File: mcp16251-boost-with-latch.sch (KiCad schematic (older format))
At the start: 26 parts

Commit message: Battery input SPDT switch
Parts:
- added SW?: SW_SPDT, symbol Switch:SW_SPDT
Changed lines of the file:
@@
 	1    0    0    1
 $EndComp
-Text GLabel 1500 1900 0    50   Input ~ 0
+Text GLabel 1100 2000 0    50   Input ~ 0
 VBAT_RAW
 Text GLabel 1900 4300 2    50   Input ~ 0
@@
 	1800 5600 1600 5600
 Connection ~ 1800 4900
+$Comp
+L Switch:SW_SPDT SW?
+U 1 1 5C07AA94
+P 1300 2000
+F 0 "SW?" H 1300 2290 50  0000 C CNN
+F 1 "SW_SPDT" H 1300 2197 50  0000 C CNN
+F 2 "" H 1300 2000 50  0001 C CNN
+F 3 "" H 1300 2000 50  0001 C CNN
+	1    1300 2000
+	1    0    0    -1
+$EndComp
 $EndSCHEMATC

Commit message: Create and assign footprints.
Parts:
- added JP1: Jumper, MCP16251_module:R_0805_HS, symbol Jumper:SolderJumper_2_Open
- C1, C2, C3, C4: renamed from C?; footprint (none) -> MCP16251_module:R_1206_HS
- C5: renamed from C?; footprint (none) -> MCP16251_module:R_0805_HS
- J1: renamed from J?; footprint (none) -> MCP16251_module:Conn_01x02_cast
- J2, J3: renamed from J?; footprint (none) -> MCP16251_module:Conn_01x02_cast_mirrored
- J4, J5, J6, J7, J8: renamed from J?; footprint (none) -> MCP16251_module:SMD-Pad_01x01
- J9: renamed from J?; footprint (none) -> Connectors_JST:JST_PH_S2B-PH-K_02x2.00mm_Angled
- L1: renamed from L?; footprint (none) -> MCP16251_module:L_Taiyo-Yuden_NR-S-40xx_HS
- Q1: renamed from Q?; footprint (none) -> MCP16251_module:SOT-23_HS
- Q2: renamed from Q?; value 2N3904 -> NPN_3904; footprint (none) -> MCP16251_module:SOT-23_HS
- R1, R2, R3, R4, R5, R6: renamed from R?; footprint (none) -> MCP16251_module:R_0805_HS
- RV1: renamed from RV?; footprint (none) -> MCP16251_module:Conn_01x03_small
- SW1: renamed from SW?; footprint (none) -> MCP16251_module:Conn_01x03_small
- SW2: renamed from SW?; footprint (none) -> Buttons_Switches_SMD:SW_SPST_TL3342
- U1: renamed from U?; footprint (none) -> MCP16251_module:SOT-23-6_HS
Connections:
- wire segments 64 -> 71
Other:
- moved on the sheet: SW1

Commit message: Bugfixes
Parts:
- J3: footprint MCP16251_module:Conn_01x02_cast_mirrored -> MCP16251_module:Conn_01x01_cast
- Q2: symbol Device:Q_NPN_EBC -> Device:Q_NPN_BEC
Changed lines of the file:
@@
 $EndComp
 $Comp
-L Device:Q_NPN_EBC Q2
+L Device:Q_NPN_BEC Q2
 U 1 1 5C03897A
 P 3300 2700
@@
 F 0 "J3" H 6379 4342 50  0000 L CNN
 F 1 "THT_Castellated" H 6379 4249 50  0000 L CNN
-F 2 "MCP16251_module:Conn_01x02_cast_mirrored" H 6300 4300 50  0001 C CNN
+F 2 "MCP16251_module:Conn_01x01_cast" H 6300 4300 50  0001 C CNN
 F 3 "~" H 6300 4300 50  0001 C CNN
 	1    6300 4300

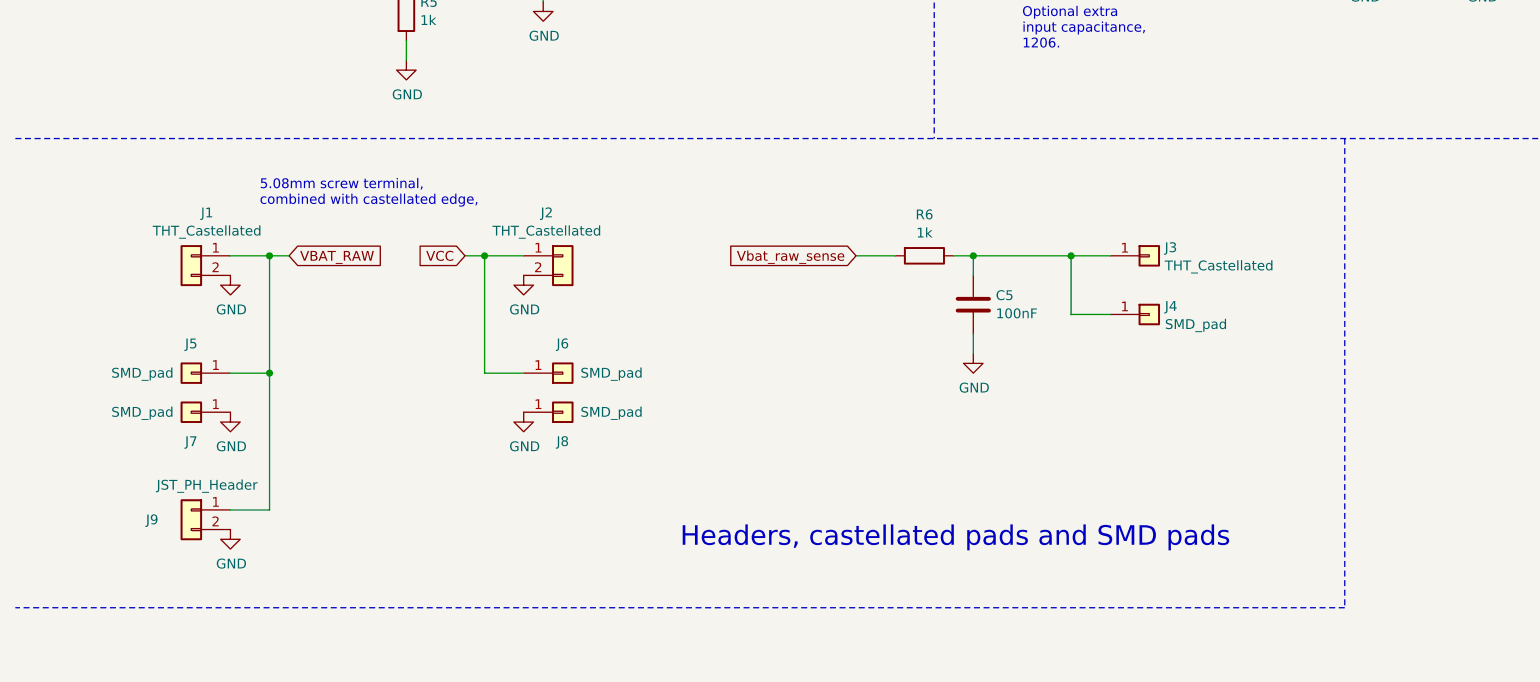
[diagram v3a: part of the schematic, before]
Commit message: Try alternative (more square-ish) layout
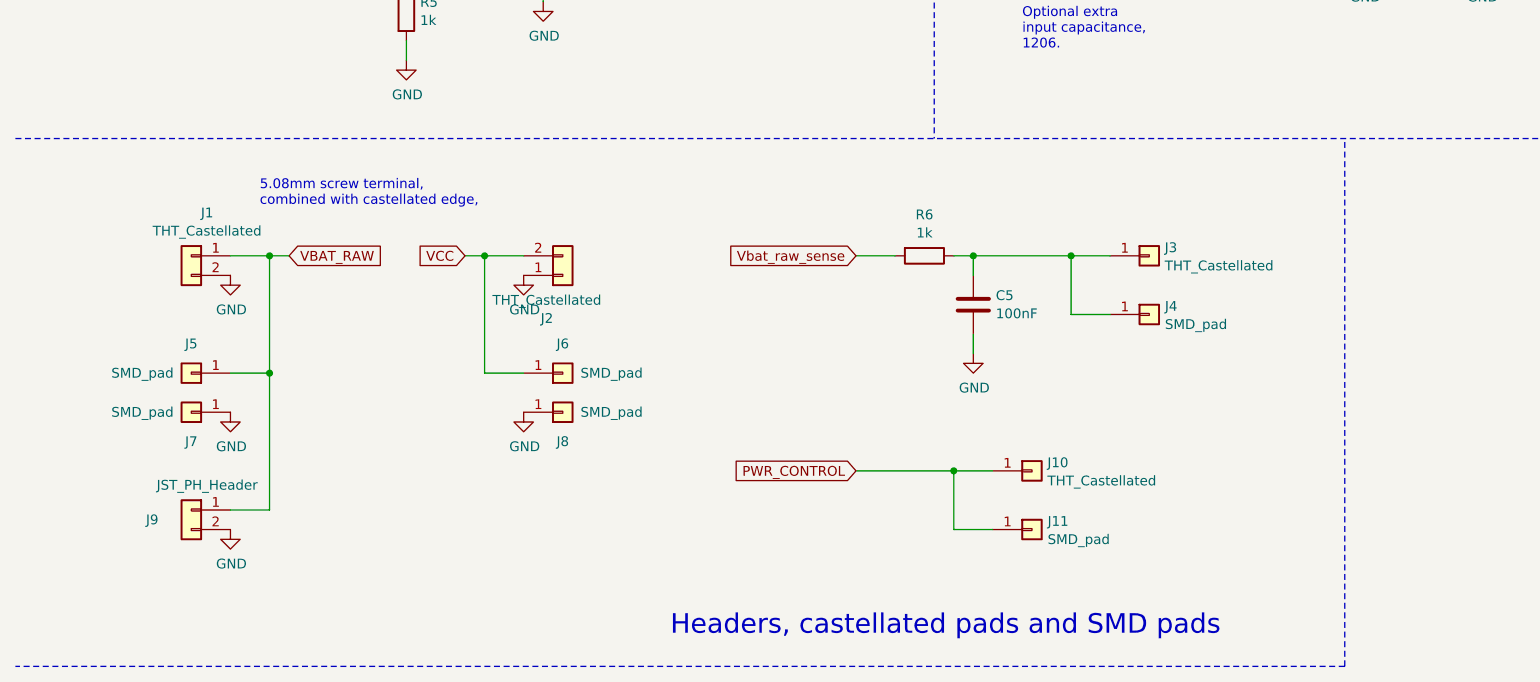
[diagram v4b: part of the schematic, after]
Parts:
- added J10: THT_Castellated, MCP16251_module:Conn_01x01_cast, symbol Connector_Generic:Conn_01x01
- added J11: SMD_pad, MCP16251_module:SMD-Pad_01x01, symbol Connector_Generic:Conn_01x01
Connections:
- net GND: now also J2.1 (Pin_1); no longer J2.2 (Pin_2)
- net PWR_CONTROL: now also J10.1 (Pin_1), J11.1 (Pin_1)
- net VCC: now also J2.2 (Pin_2); no longer J2.1 (Pin_1)
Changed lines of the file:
@@
 L Connector_Generic:Conn_01x02 J2
 U 1 1 5C0585BB
-P 3300 4300
-F 0 "J2" H 3219 4520 50  0000 C CNN
-F 1 "THT_Castellated" H 3219 4427 50  0000 C CNN
-F 2 "MCP16251_module:Conn_01x02_cast_mirrored" H 3300 4300 50  0001 C CNN
-F 3 "~" H 3300 4300 50  0001 C CNN
-	1    3300 4300
-	1    0    0    -1
+P 3300 4400
+F 0 "J2" H 3219 4620 50  0000 C CNN
+F 1 "THT_Castellated" H 3219 4527 50  0000 C CNN
+F 2 "MCP16251_module:Conn_01x02_cast_mirrored" H 3300 4400 50  0001 C CNN
+F 3 "~" H 3300 4400 50  0001 C CNN
+	1    3300 4400
+	1    0    0    1
 $EndComp
 $Comp
@@
 Wire Wire Line
 	2900 4300 3100 4300
-Text Notes 3900 5800 0    100  ~ 0
+Text Notes 3850 6250 0    100  ~ 0
 Headers, castellated pads and SMD pads
 Wire Notes Line
-	7300 3700 7300 6100
-Wire Notes Line
-	7300 6100 500  6100
+	7300 6400 500  6400
 $Comp
 L Connector_Generic:Conn_01x02 J9
@@
 Wire Wire Line
 	1600 1700 1800 1700
+Text GLabel 4800 5400 0    50   Input ~ 0
+PWR_CONTROL
+$Comp
+L Connector_Generic:Conn_01x01 J10
+U 1 1 5C08B0BD
+P 5700 5400
+F 0 "J10" H 5779 5442 50  0000 L CNN
+F 1 "THT_Castellated" H 5779 5349 50  0000 L CNN
+F 2 "MCP16251_module:Conn_01x01_cast" H 5700 5400 50  0001 C CNN
+F 3 "~" H 5700 5400 50  0001 C CNN
+	1    5700 5400
+	1    0    0    -1
+$EndComp
+$Comp
+L Connector_Generic:Conn_01x01 J11
+U 1 1 5C08B0C3
+P 5700 5700
+F 0 "J11" H 5780 5742 50  0000 L CNN
+F 1 "SMD_pad" H 5780 5649 50  0000 L CNN
+F 2 "MCP16251_module:SMD-Pad_01x01" H 5700 5700 50  0001 C CNN
+F 3 "~" H 5700 5700 50  0001 C CNN
+	1    5700 5700
+	1    0    0    -1
+$EndComp
+Wire Wire Line
+	4800 5400 5300 5400
+Wire Wire Line
+	5300 5400 5300 5700
+Wire Wire Line
+	5300 5700 5500 5700
+Connection ~ 5300 5400
+Wire Wire Line
+	5300 5400 5500 5400
+Wire Notes Line
+	7300 6400 7300 3700
 $EndSCHEMATC

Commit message: Include voltage supervisors for reliable start and battery protection
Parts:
- removed C3: CP1, MCP16251_module:R_1206_HS, symbol Device:CP1
- added F?: Polyfuse, symbol Device:Polyfuse
- added J?: THT_Castellated, MCP16251_module:Conn_01x01_cast, symbol Connector_Generic:Conn_01x01
- added J?: SMD_pad, MCP16251_module:SMD-Pad_01x01, symbol Connector_Generic:Conn_01x01
- added Q? (x4): Q_PMOS_GSD, symbol Device:Q_PMOS_GSD
- added Q?: Q_NPN_BEC, symbol Device:Q_NPN_BEC
- added R? (x5): 100k, MCP16251_module:R_0805_HS, symbol Device:R_Small
- added U?: MIC809, symbol _Project_Local:MIC809
- added U?: MIC803, symbol _Project_Local:MIC803
- added U? (x2): Opamp_Dual_Generic, symbol Device:Opamp_Dual_Generic
- R4: symbol Device:R -> Device:R_Small
- R5: value 1k -> 100k; symbol Device:R -> Device:R_Small
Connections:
- net GND: now also SW2.1, Q?.2 (E), R?.2, U?.1 (GND), U?.1 (GND), U?.4 (V-)
- net PWR_CONTROL: now also R5.1
- net VBAT: now also U?.3 (VCC); no longer U1.3 (EN)
- net VBAT_RAW: now also F?.2; no longer JP1.1 (A), SW1.2 (B)
- net VCC renamed 5V
- net 5V: now also R?.1, U?.2 (-), U?.3 (VCC)
- new net: F?.1, JP1.1 (A), SW1.2 (B)
- new net: Q?.1 (G), Q?.1 (G), R?.1, U?.1
- new net: Q?.1 (G), Q?.1 (G), Q?.3 (C), R?.1
- new net: Q?.2 (S), Q?.2 (S), R?.2 (x2)
- new net: Q?.1 (B), R?.1
- new net: R?.2, R?.2
- new net 3-4.2V: Q?.3 (D), Q?.3 (D), U?.3 (+), U?.8 (V+)
- new net STAGE1: R?.1, U1.3 (EN), U?.2 (~RST)
- new net STAGE2: J?.1 (Pin_1), J?.1 (Pin_1), U?.2 (~RST)
- new net uC_ADC: Q?.3 (D), Q?.3 (D)
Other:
- note added: "750mA\n1206"
- note added: "Power supply headers,\ncastellated and SMD pads"
- note added: "Power-on/off\ncontrol header"
- note added: "Raw VBAT input, power-off circuit,\nvoltage supervisor for boost converter"
- note added: "THT_Castellated = 5.08mm screw terminal,\ncombined with castellated edge"
- note added: "TODO: needs fixing!"
- note added: "To RESET pin on microcontroller"
- note added: "Voltage supervisor for microcontroller"
- note added: "Vth = 2.93V"
- note added: "open-drain"
- note added: "or 10uF"
- note removed: "5.08mm screw terminal,\ncombined with castellated edge,"
- note removed: "Headers, castellated pads and SMD pads"
- note removed: "Optional extra\ninput capacitance,\n1206."
- note removed: "Raw VBAT input, voltage sense\nand auto power-off"
- moved on the sheet: C1, C2, C4, C5, J1, J10, J11, J2, J3, J4, J5, J6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

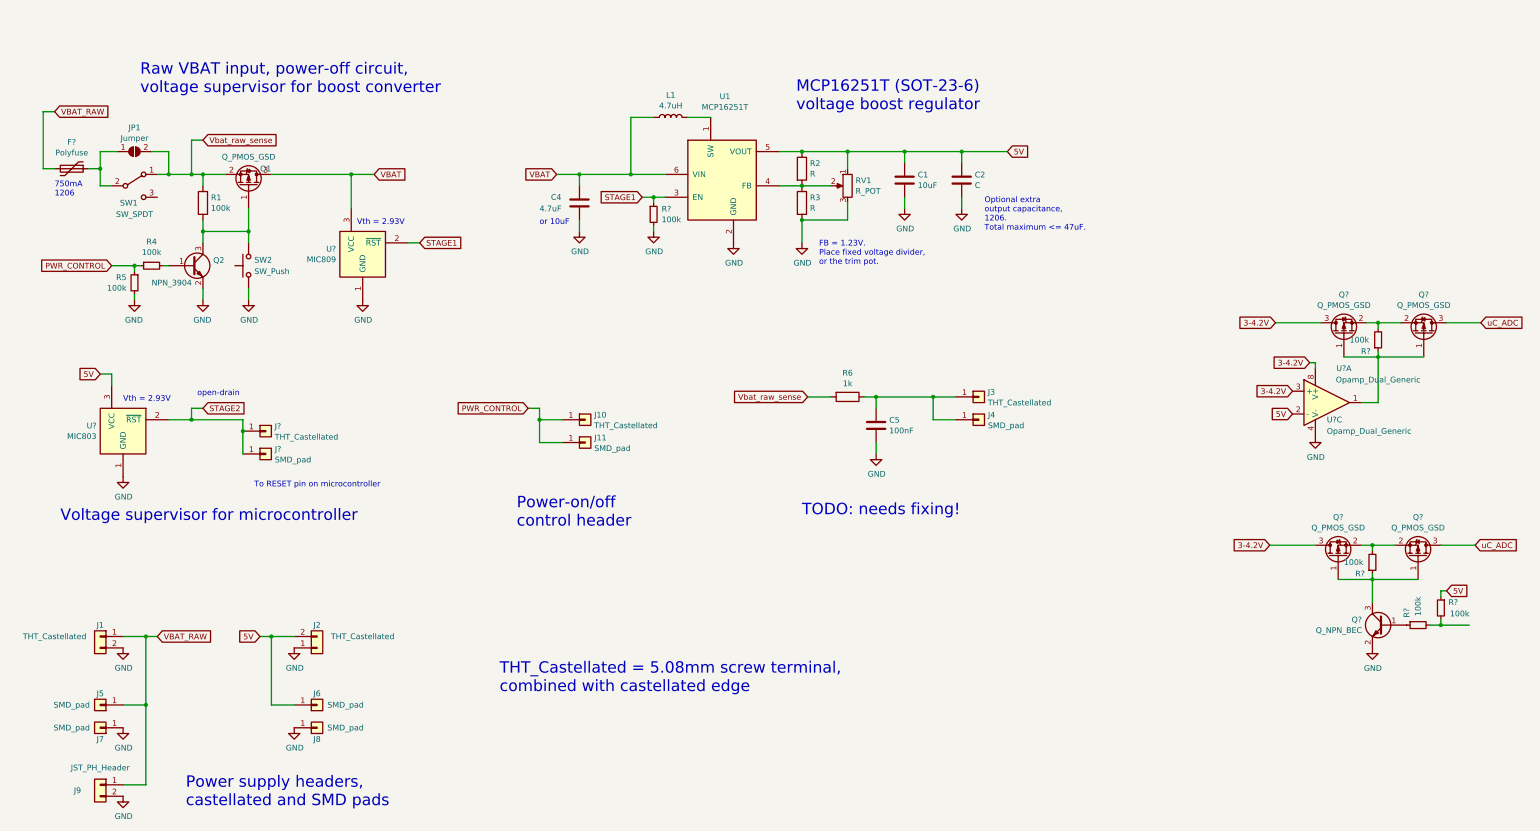
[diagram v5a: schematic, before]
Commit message: VBAT sense switch using Back-to-back P-MOSFET enabled by MIC2777
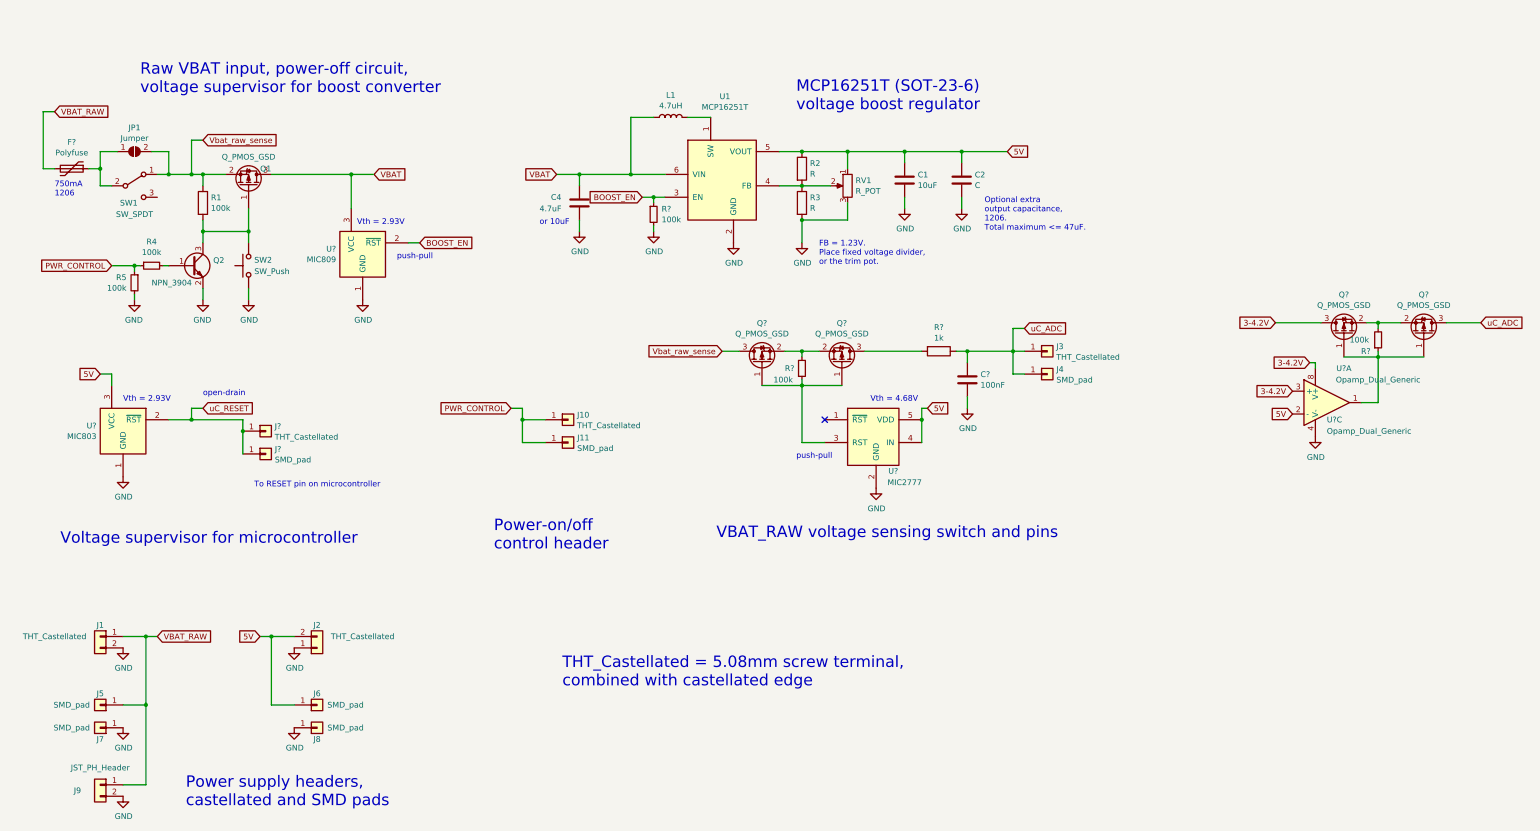
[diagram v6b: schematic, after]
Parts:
- removed C5: 100nF, MCP16251_module:R_0805_HS, symbol Device:C
- removed Q?: Q_NPN_BEC, symbol Device:Q_NPN_BEC
- removed R6: 1k, MCP16251_module:R_0805_HS, symbol Device:R
- removed R? (x2): 100k, MCP16251_module:R_0805_HS, symbol Device:R_Small
- added C?: 100nF, MCP16251_module:R_0805_HS, symbol Device:C
- added R?: 1k, MCP16251_module:R_0805_HS, symbol Device:R
- added U?: MIC2777, symbol _Project_Local:MIC2777
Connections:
- net 3-4.2V: no longer Q?.3 (D)
- net 5V: now also U?.4 (IN), U?.5 (VDD)
- net GND: now also C?.2, U?.2 (GND)
- net Vbat_raw_sense: now also Q?.3 (D)
- net uC_ADC: now also J3.1 (Pin_1), J4.1 (Pin_1), C?.1, R?.1; no longer Q?.3 (D)
- net at Q?.1 (G), Q?.1 (G), R?.1: now also U?.3 (RST)
- net STAGE1 renamed BOOST_EN
- net STAGE2 renamed uC_RESET
- new net: Q?.3 (D), R?.2
- no-connect marks 0 -> 1
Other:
- note added: "VBAT_RAW voltage sensing switch and pins"
- note added: "Vth = 4.68V"
- note added: "push-pull"
- note removed: "TODO: needs fixing!"
- moved on the sheet: J10, J11, J3, J4, Q?, R?

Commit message: Clean up schematic
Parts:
- removed Q? (x2): Q_PMOS_GSD, symbol Device:Q_PMOS_GSD
- removed R?: 100k, MCP16251_module:R_0805_HS, symbol Device:R_Small
- removed U? (x2): Opamp_Dual_Generic, symbol Device:Opamp_Dual_Generic
- gave numbers to parts that had none: 12
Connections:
- net 5V: no longer U4.4 (IN)
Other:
- moved on the sheet: C4, J12, J13
